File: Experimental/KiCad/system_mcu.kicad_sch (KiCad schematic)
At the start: 62 parts, among them IC1 SN74HCS02PWR, IC2 TPS3851H18EDRBR, IC3 M24C32-DFDW6TP, IC4 STM32G071R8T6, IC5 TPA6205A1DGN, Q2 2N7002, Q3 MMBT5401, Y1 32.768KHz

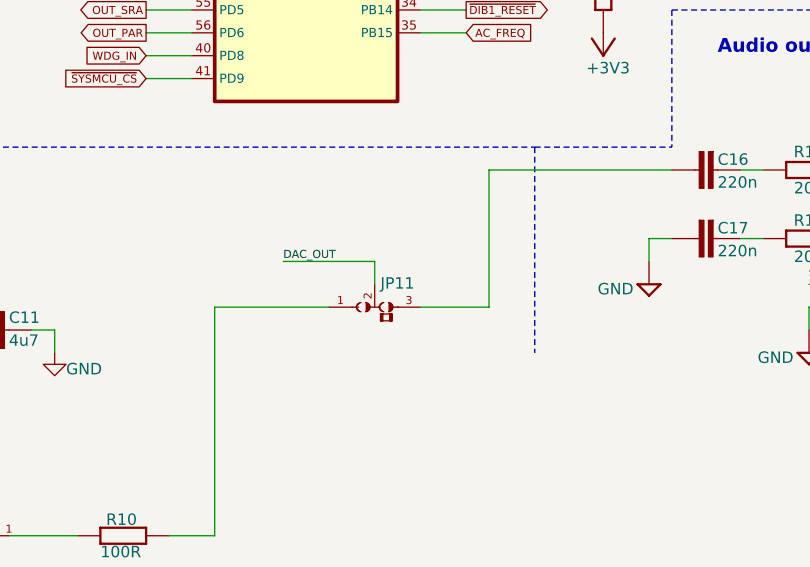
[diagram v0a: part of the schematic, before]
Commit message: BOM update, small changes
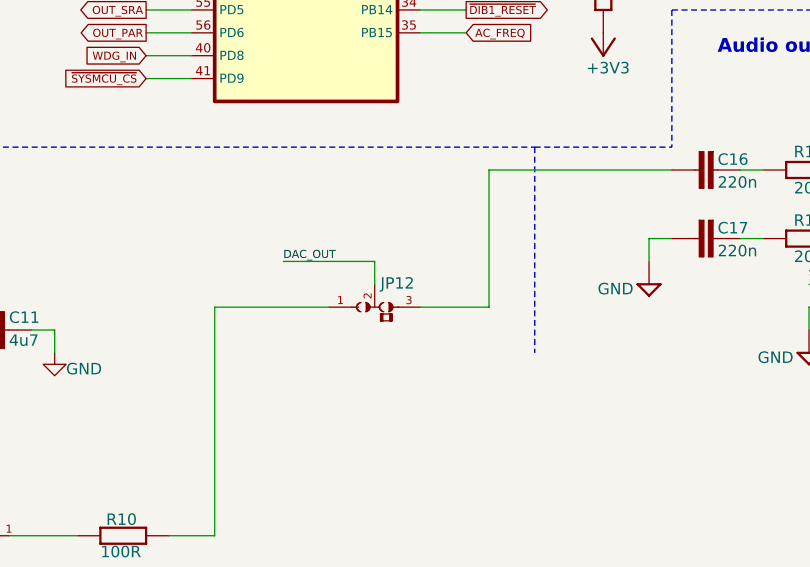
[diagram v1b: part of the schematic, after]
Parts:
- renumbered JP11 to JP12
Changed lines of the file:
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@@
 	(title_block
 		(title "BB3+ test mainboard")
-		(date "2025-10-11")
+		(date "2025-10-12")
 		(rev "r1B1")
 		(company "Envox d.o.o.")
@@
 		(on_board yes)
 		(dnp no)
-		(property "Reference" "JP11"
+		(property "Reference" "JP12"
 			(at 160.655 155.575 0)
 			(effects
@@
 			(project "BB3plus MCU test board"
 				(path "/1df84e4f-233a-4f72-9418-c0020706bb76/fecdace5-b1da-40fa-9e4e-3a9b862ce872"
-					(reference "JP11")
+					(reference "JP12")
 					(unit 1)
 				)

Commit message: Update project info
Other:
- company: Envox d.o.o. -> ${project_creator}
- title: BB3+ test mainboard -> ${project_name}
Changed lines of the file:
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@@
 	(paper "A4")
 	(title_block
-		(title "BB3+ test mainboard")
-		(date "2025-10-12")
-		(rev "r1B1")
-		(company "Envox d.o.o.")
-		(comment 1 "Licensed under the TAPR Open Hardware License (www.tapr.org/OHL)")
-		(comment 2 "More info at http://www.envox.eu/")
+		(title "${project_name}")
+		(date "2025-10-13")
+		(rev "${project_version}")
+		(company "${project_creator}")
+		(comment 1 "${project_license}")
+		(comment 2 "${project_info}")
 	)
 	(text "Watchdog/supervisor"

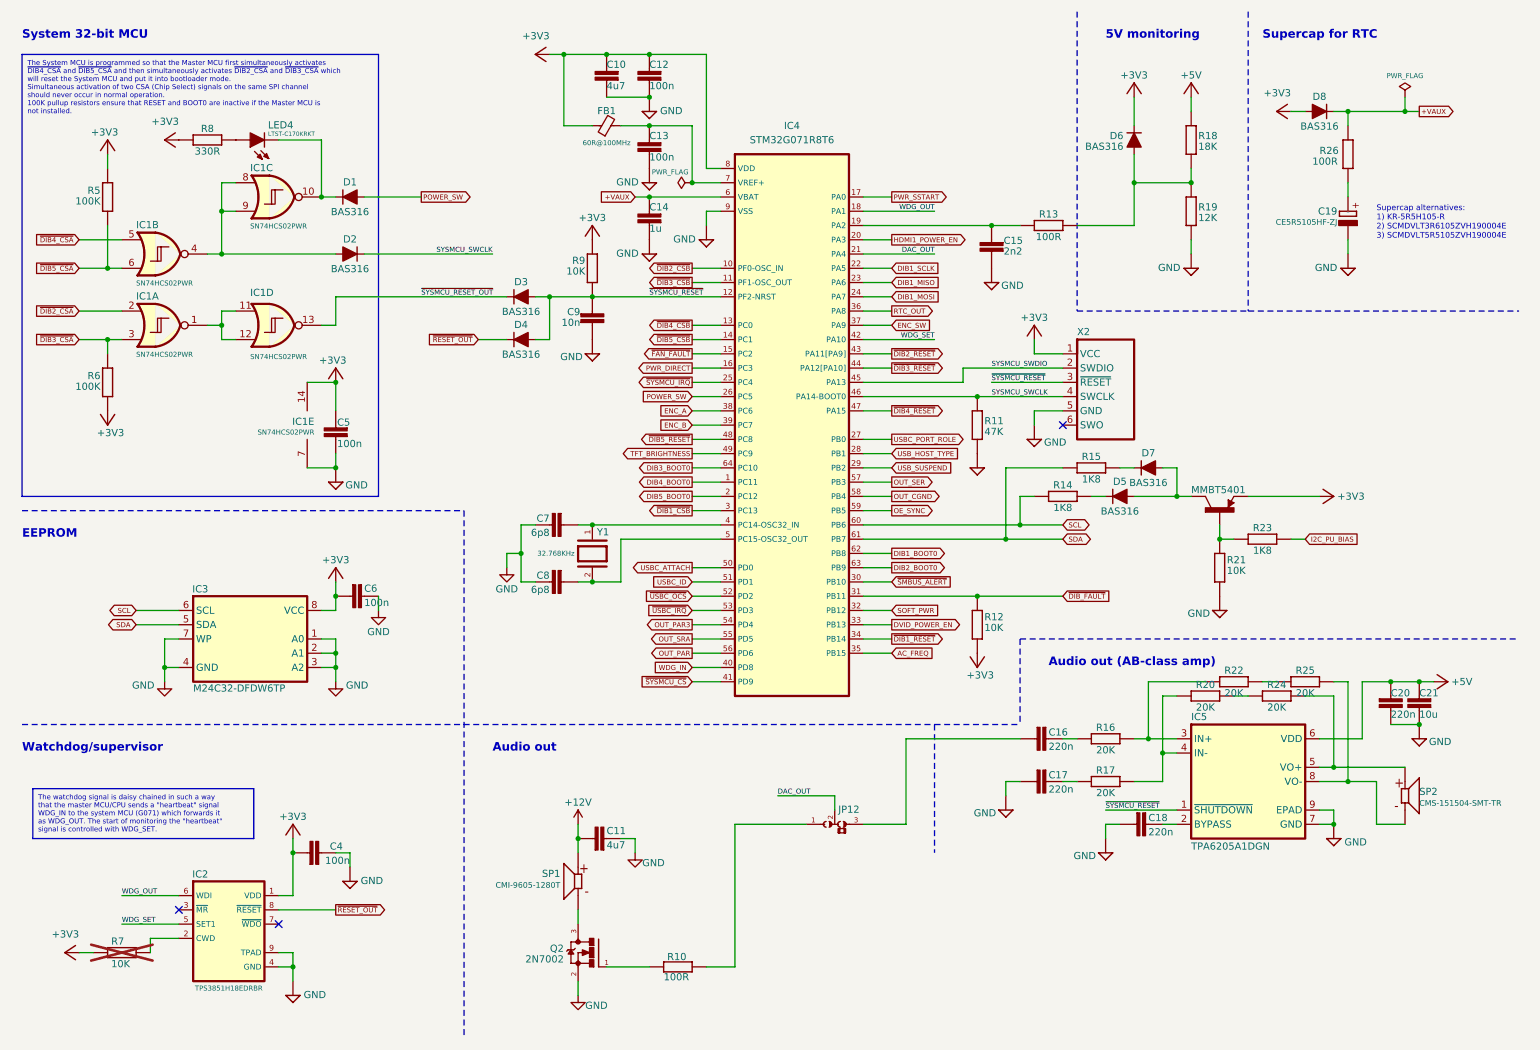
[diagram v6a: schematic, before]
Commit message: Replace 3V3 jumper for H7 CM5 with PMOS sw
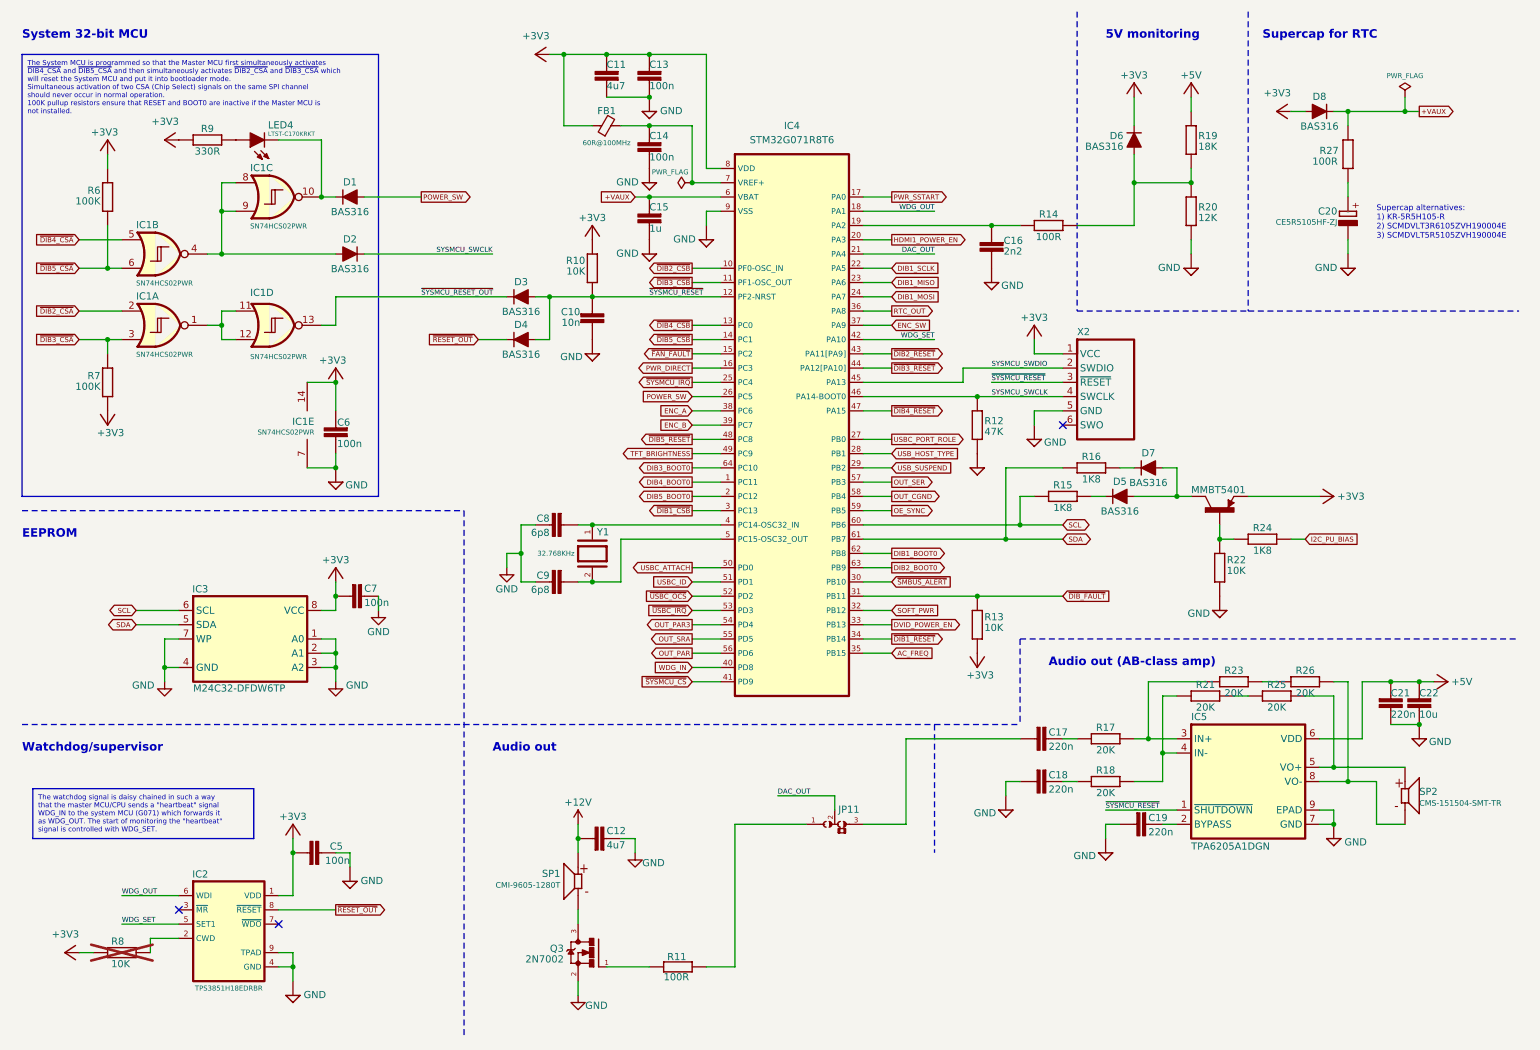
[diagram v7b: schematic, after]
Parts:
- renumbered C9 to C10, C10 to C11, C11 to C12, C12 to C13, C13 to C14, C14 to C15, C15 to C16, C16 to C17, C17 to C18, C18 to C19, C19 to C20, C20 to C21, C21 to C22, C4 to C5, C5 to C6, C6 to C7, C7 to C8, C8 to C9, JP12 to JP11, Q2 to Q3, Q3 to Q4, R9 to R10, R10 to R11, R11 to R12, R12 to R13, R13 to R14, R14 to R15, R15 to R16, R16 to R17, R17 to R18, R18 to R19, R19 to R20, R20 to R21, R21 to R22, R22 to R23, R23 to R24, R24 to R25, R25 to R26, R26 to R27, R5 to R6, R6 to R7, R7 to R8, R8 to R9

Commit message: Jumpers update
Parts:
- JP11: symbol PCM_EEZ_unsorted:JP3 shorted with 0R (2-3) -> PCM_EEZ_unsorted:JP3 2mm THT (2-3)
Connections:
- net I2C_PU_BIAS renamed CM5_3V3
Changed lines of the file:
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@@
 	(title_block
 		(title "${project_name}")
-		(date "2025-10-19")
+		(date "2025-10-21")
 		(rev "${project_version}")
 		(company "${project_creator}")
@@
 	(wire
 		(pts
-			(xy 165.1 157.48) (xy 172.72 157.48)
+			(xy 162.56 157.48) (xy 172.72 157.48)
 		)
 		(stroke
@@
 	(wire
 		(pts
-			(xy 142.24 157.48) (xy 154.94 157.48)
+			(xy 142.24 157.48) (xy 157.48 157.48)
 		)
 		(stroke
@@
 		)
 	)
-	(global_label "I2C_PU_BIAS"
+	(global_label "CM5_3V3"
 		(shape input)
 		(at 243.84 106.68 0)
@@
 		)
 		(property "Intersheetrefs" "${INTERSHEET_REFS}"
-			(at 253.7265 106.68 0)
+			(at 251.356 106.68 0)
 			(effects
 				(font
@@
 	)
 	(symbol
-		(lib_id "PCM_EEZ_unsorted:JP3 shorted with 0R (2-3)")
-		(at 160.02 157.48 0)
+		(lib_id "PCM_EEZ_unsorted:JP3 2mm THT (2-3)")
+		(at 157.48 157.48 0)
 		(mirror x)
 		(unit 1)
@@
 		(dnp no)
 		(property "Reference" "JP11"
-			(at 160.655 155.575 0)
+			(at 158.115 155.575 0)
 			(effects
 				(font
@@
 		)
 		(property "Value" "~"
-			(at 160.02 157.48 0)
+			(at 157.48 157.48 0)
 			(effects
 				(font
@@
 		)
 		(property "Footprint" "PCM_EEZ_connectors:M22-2010346"
-			(at 160.02 153.67 0)
+			(at 157.48 154.94 0)
 			(effects
 				(font
@@
 		)
 		(property "Datasheet" ""
-			(at 160.02 157.48 90)
+			(at 157.48 157.48 0)
 			(effects
 				(font
@@
 		)
 		(property "Description" ""
-			(at 160.02 157.48 0)
+			(at 157.48 157.48 0)
 			(effects
 				(font
@@
 		)
 		(property "DigiKey" "M22-2010346-ND"
-			(at 160.02 157.48 0)
+			(at 157.48 152.4 0)
+			(show_name yes)
 			(effects
 				(font
@@
 		)
 		(property "Mouser" "855-M22-2010346"
-			(at 160.02 157.48 0)
+			(at 157.48 149.86 0)
+			(show_name yes)
 			(effects
 				(font
@@
 		)
 		(property "TME" "-"
-			(at 160.02 157.48 0)
+			(at 157.48 147.32 0)
+			(show_name yes)
 			(effects
 				(font
@@
 		)
 		(property "LCSC" "C6658749"
-			(at 160.02 157.48 0)
+			(at 157.48 144.78 0)
+			(show_name yes)
 			(effects
 				(font
@@
 		)
 		(property "Label" "AUDIO SEL"
-			(at 160.02 157.48 90)
+			(at 157.48 157.48 90)
 			(effects
 				(font
